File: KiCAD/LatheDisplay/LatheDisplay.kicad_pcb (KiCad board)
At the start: 2 copper layers, 5 parts, among them U1 D168K, U2 D168K, U3 D168K, U4 D168K, U5 D168K

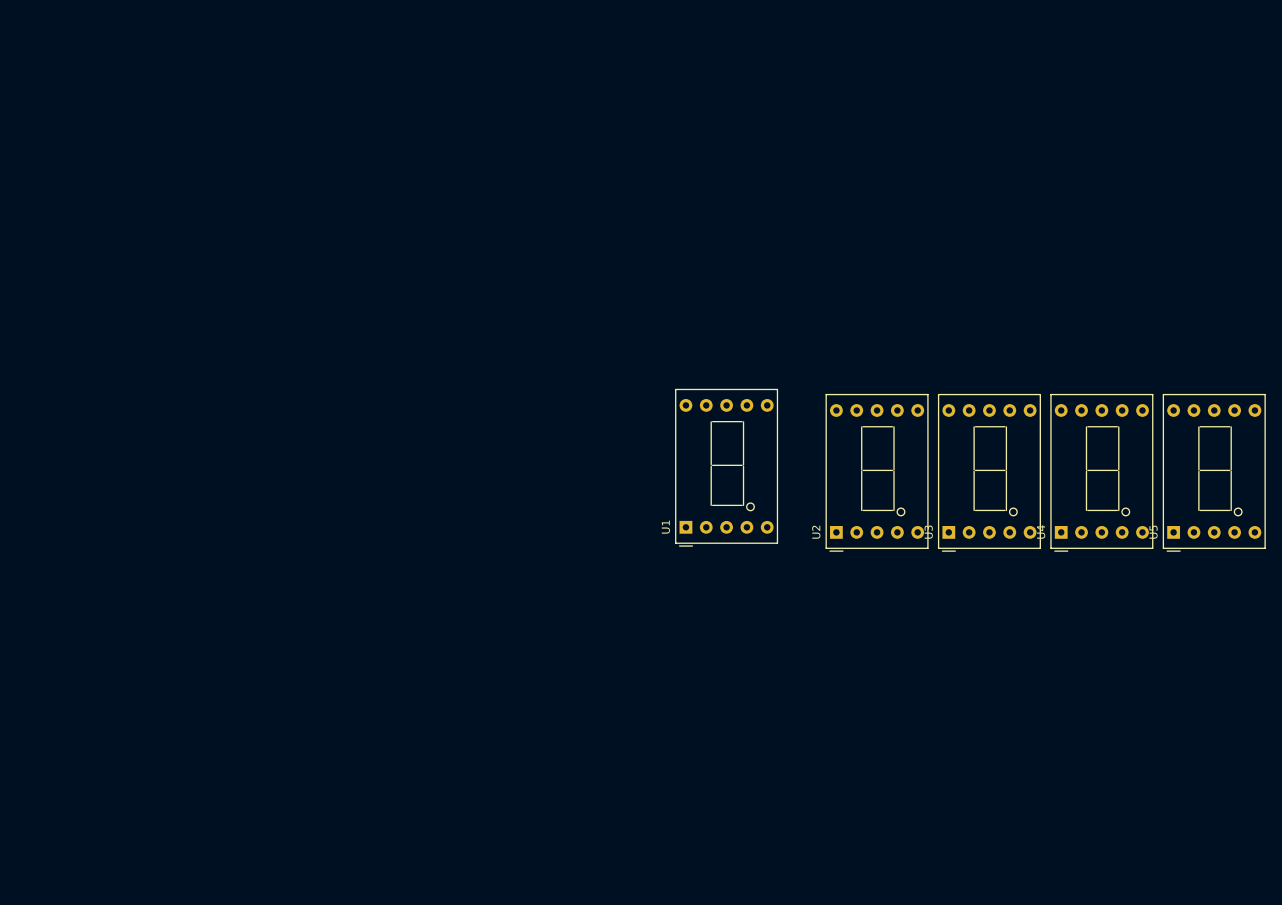
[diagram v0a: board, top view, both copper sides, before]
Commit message: components assigned and tentative placement
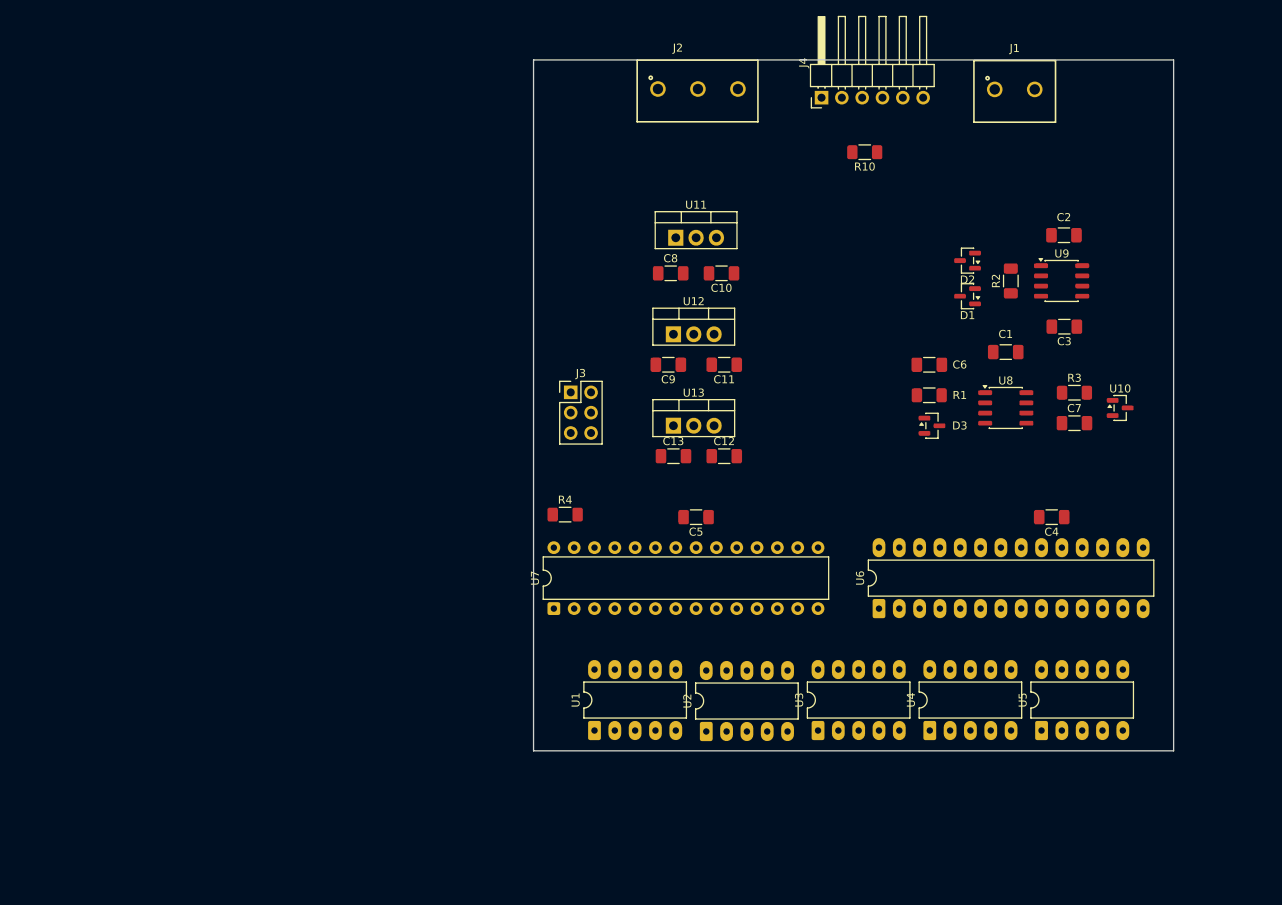
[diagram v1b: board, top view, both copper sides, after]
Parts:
- added C1: 0.1uF, Capacitor_SMD:C_1206_3216Metric_Pad1.33x1.80mm_HandSolder, F.Cu at (179.7, 75.9)
- added C10: 0.1uF, Capacitor_SMD:C_1206_3216Metric_Pad1.33x1.80mm_HandSolder, F.Cu at (144.1, 66.0)
- added C11: 0.1uF, Capacitor_SMD:C_1206_3216Metric_Pad1.33x1.80mm_HandSolder, F.Cu at (144.5, 77.5)
- added C12: 0.1uF, Capacitor_SMD:C_1206_3216Metric_Pad1.33x1.80mm_HandSolder, F.Cu at (144.5, 88.9)
- added C13: 0.1uF, Capacitor_SMD:C_1206_3216Metric_Pad1.33x1.80mm_HandSolder, F.Cu at (138.1, 88.9)
- added C2: 0.1uF, Capacitor_SMD:C_1206_3216Metric_Pad1.33x1.80mm_HandSolder, F.Cu at (187.0, 61.3)
- added C3: 0.1uF, Capacitor_SMD:C_1206_3216Metric_Pad1.33x1.80mm_HandSolder, F.Cu at (187.0, 72.7)
- added C4: 0.1uF, Capacitor_SMD:C_1206_3216Metric_Pad1.33x1.80mm_HandSolder, F.Cu at (185.4, 96.5)
- added C5: 0.1uF, Capacitor_SMD:C_1206_3216Metric_Pad1.33x1.80mm_HandSolder, F.Cu at (141.0, 96.5)
- added C6: 0.1uF, Capacitor_SMD:C_1206_3216Metric_Pad1.33x1.80mm_HandSolder, F.Cu at (170.1, 77.5)
- added C7: 0.1uF, Capacitor_SMD:C_1206_3216Metric_Pad1.33x1.80mm_HandSolder, F.Cu at (188.3, 84.8)
- added C8: 0.1uF, Capacitor_SMD:C_1206_3216Metric_Pad1.33x1.80mm_HandSolder, F.Cu at (137.8, 66.0)
- added C9: 0.1uF, Capacitor_SMD:C_1206_3216Metric_Pad1.33x1.80mm_HandSolder, F.Cu at (137.5, 77.5)
- added D1: BAV99, Package_TO_SOT_SMD:SOT-23, F.Cu at (174.9, 68.9)
- added D2: BAV99, Package_TO_SOT_SMD:SOT-23, F.Cu at (174.9, 64.5)
- added D3: BAV99, Package_TO_SOT_SMD:SOT-23, F.Cu at (170.5, 85.1)
- added J1: Screw_Terminal_01x02, models:691137710002, F.Cu at (180.8, 43.0)
- added J2: Screw_Terminal_01x03, models:3-pin-terminal, F.Cu at (138.7, 43.0)
- added J3: AVR-ISP-6, Connector_PinHeader_2.54mm:PinHeader_2x03_P2.54mm_Vertical, F.Cu at (125.3, 80.9)
- added J4: Conn_01x06_Pin, Connector_PinHeader_2.54mm:PinHeader_1x06_P2.54mm_Horizontal, F.Cu at (156.7, 44.1)
- added R1: 1k, Resistor_SMD:R_1206_3216Metric_Pad1.30x1.75mm_HandSolder, F.Cu at (170.1, 81.3)
- added R10: 0R, Resistor_SMD:R_1206_3216Metric_Pad1.30x1.75mm_HandSolder, F.Cu at (162.1, 50.9)
- added R2: RGAIN, Resistor_SMD:R_1206_3216Metric_Pad1.30x1.75mm_HandSolder, F.Cu at (180.3, 67.0)
- added R3: 2k, Resistor_SMD:R_1206_3216Metric_Pad1.30x1.75mm_HandSolder, F.Cu at (188.3, 81.0)
- added R4: 2k, Resistor_SMD:R_1206_3216Metric_Pad1.30x1.75mm_HandSolder, F.Cu at (124.6, 96.2)
- added U10: LM4040DBZ-4.1, Package_TO_SOT_SMD:SOT-23, F.Cu at (194.0, 82.9)
- added U11: LM7812_TO220, Package_TO_SOT_THT:TO-220-3_Vertical, F.Cu at (138.4, 61.6)
- added U12: LM7912_TO220, Package_TO_SOT_THT:TO-220-3_Vertical, F.Cu at (138.1, 73.7)
- added U13: LM7805_TO220, Package_TO_SOT_THT:TO-220-3_Vertical, F.Cu at (138.1, 85.1)
- added U6: ICM7218B, Package_DIP:DIP-28_W7.62mm_LongPads, F.Cu at (163.8, 108.0)
- added U7: ATmega328-P, Package_DIP:DIP-28_W7.62mm, F.Cu at (123.2, 108.0)
- added U8: TLC3541, Package_SO:SO-8_3.9x4.9mm_P1.27mm, F.Cu at (179.7, 82.9)
- added U9: INA121, Package_SO:SO-8_3.9x4.9mm_P1.27mm, F.Cu at (186.7, 67.0)
- U1, U2, U3, U4, U5: footprint Display_7Segment:D1X8K -> Package_DIP:DIP-10_W7.62mm_LongPads
- moved U5 29.8 mm to (184.2, 123.2)
- moved U2 29.7 mm to (142.2, 123.3)
- moved U4 29.7 mm to (170.2, 123.2)
- moved U3 29.7 mm to (156.2, 123.2)
- moved U1 27.9 mm to (128.3, 123.2)
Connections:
- U1 pad 1: unconnected-(U1-E-Pad1) -> /SE
- U1 pad 10: unconnected-(U1-G-Pad10) -> /SG
- U1 pad 2: unconnected-(U1-D-Pad2) -> /SD
- U1 pad 3: unconnected-(U1-CC-Pad3) -> Net-(U6-d1)
- U1 pad 4: unconnected-(U1-C-Pad4) -> /SC
- U1 pad 5: unconnected-(U1-DP-Pad5) -> /DP
- U1 pad 6: unconnected-(U1-B-Pad6) -> /SB
- U1 pad 7: unconnected-(U1-A-Pad7) -> /SA
- U1 pad 8: unconnected-(U1-CC-Pad8) -> Net-(U6-d1)
- U1 pad 9: unconnected-(U1-F-Pad9) -> /SF
- U2 pad 1: unconnected-(U2-E-Pad1) -> /SE
- U2 pad 10: unconnected-(U2-G-Pad10) -> /SG
- U2 pad 2: unconnected-(U2-D-Pad2) -> /SD
- U2 pad 3: unconnected-(U2-CC-Pad3) -> Net-(U6-d2)
- U2 pad 4: unconnected-(U2-C-Pad4) -> /SC
- U2 pad 5: unconnected-(U2-DP-Pad5) -> /DP
- U2 pad 6: unconnected-(U2-B-Pad6) -> /SB
- U2 pad 7: unconnected-(U2-A-Pad7) -> /SA
- U2 pad 8: unconnected-(U2-CC-Pad8) -> Net-(U6-d2)
- U2 pad 9: unconnected-(U2-F-Pad9) -> /SF
- U3 pad 1: unconnected-(U3-E-Pad1) -> /SE
- U3 pad 10: unconnected-(U3-G-Pad10) -> /SG
- U3 pad 2: unconnected-(U3-D-Pad2) -> /SD
- U3 pad 3: unconnected-(U3-CC-Pad3) -> Net-(U6-d3)
- U3 pad 4: unconnected-(U3-C-Pad4) -> /SC
- U3 pad 5: unconnected-(U3-DP-Pad5) -> /DP
- U3 pad 6: unconnected-(U3-B-Pad6) -> /SB
- U3 pad 7: unconnected-(U3-A-Pad7) -> /SA
- U3 pad 8: unconnected-(U3-CC-Pad8) -> Net-(U6-d3)
- U3 pad 9: unconnected-(U3-F-Pad9) -> /SF
- U4 pad 1: unconnected-(U4-E-Pad1) -> /SE
- U4 pad 10: unconnected-(U4-G-Pad10) -> /SG
- U4 pad 2: unconnected-(U4-D-Pad2) -> /SD
- U4 pad 3: unconnected-(U4-CC-Pad3) -> Net-(U6-d4)
- U4 pad 4: unconnected-(U4-C-Pad4) -> /SC
- U4 pad 5: unconnected-(U4-DP-Pad5) -> /DP
- U4 pad 6: unconnected-(U4-B-Pad6) -> /SB
- U4 pad 7: unconnected-(U4-A-Pad7) -> /SA
- U4 pad 8: unconnected-(U4-CC-Pad8) -> Net-(U6-d4)
- U4 pad 9: unconnected-(U4-F-Pad9) -> /SF
- U5 pad 1: unconnected-(U5-E-Pad1) -> /SE
- U5 pad 10: unconnected-(U5-G-Pad10) -> /SG
- U5 pad 2: unconnected-(U5-D-Pad2) -> /SD
- U5 pad 3: unconnected-(U5-CC-Pad3) -> Net-(U6-d5)
- U5 pad 4: unconnected-(U5-C-Pad4) -> /SC
- U5 pad 5: unconnected-(U5-DP-Pad5) -> /DP
- U5 pad 6: unconnected-(U5-B-Pad6) -> /SB
- U5 pad 7: unconnected-(U5-A-Pad7) -> /SA
- U5 pad 8: unconnected-(U5-CC-Pad8) -> Net-(U6-d5)
- U5 pad 9: unconnected-(U5-F-Pad9) -> /SF
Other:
- board outline added: 80 x 86.4 mm

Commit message: save lathe stuff
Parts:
- J4: footprint Connector_PinHeader_2.54mm:PinHeader_1x06_P2.54mm_Horizontal -> Connector_PinHeader_2.54mm:PinHeader_1x06_P2.54mm_Vertical
- R1: value 1k -> 2k
- moved D1 120.6 mm to (58.7, 101.2)
- moved D2 120.6 mm to (58.7, 96.8)
- moved C3 120.6 mm to (70.8, 105.0)
- moved R2 120.6 mm to (64.1, 99.3)
- moved U9 120.6 mm to (70.5, 99.3)
- moved C2 120.6 mm to (70.8, 93.6)
- moved J1 117.5 mm to (70.7, 83.8)
- moved C1 91.2 mm to (90.7, 95.6)
- moved C6 90.6 mm to (81.3, 95.4)
- moved R1 90.6 mm to (81.3, 99.2)
- moved U8 90.6 mm to (90.8, 100.8)
- moved D3 90.6 mm to (81.6, 103.0)
- moved C7 89.7 mm to (98.8, 91.1)
- moved R3 89.7 mm to (98.8, 87.3)
- moved U10 89.7 mm to (104.5, 89.2)
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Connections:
- R10 pad 1: VCC -> +5V
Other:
- board size 80 x 86.4 mm -> 85.7 x 63.5 mm
